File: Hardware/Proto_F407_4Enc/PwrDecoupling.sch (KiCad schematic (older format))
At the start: 35 parts, among them U2 AMS1117-3.3

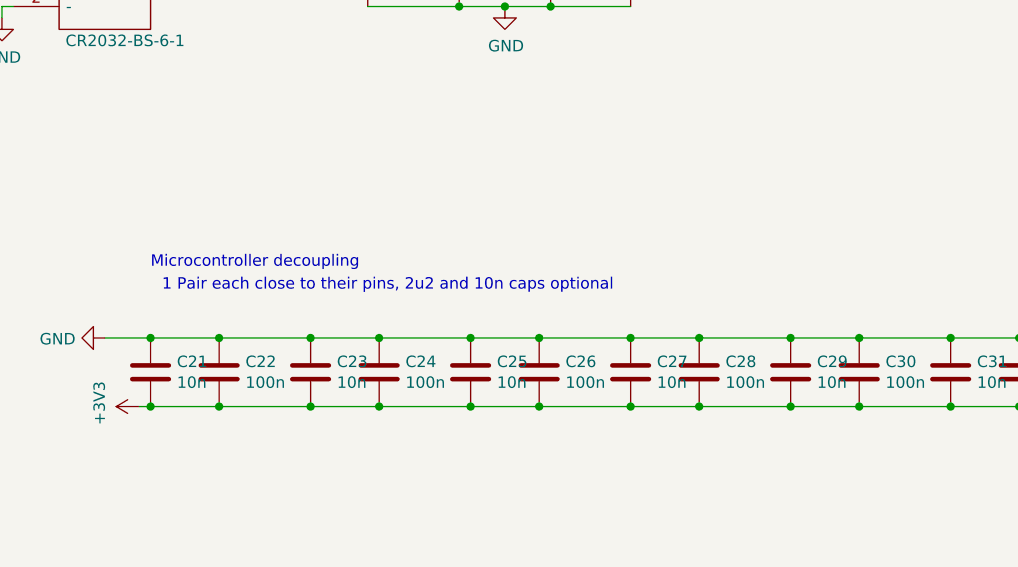
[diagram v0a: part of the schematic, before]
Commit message: minor label changes in schematic, added schematic + board image plots
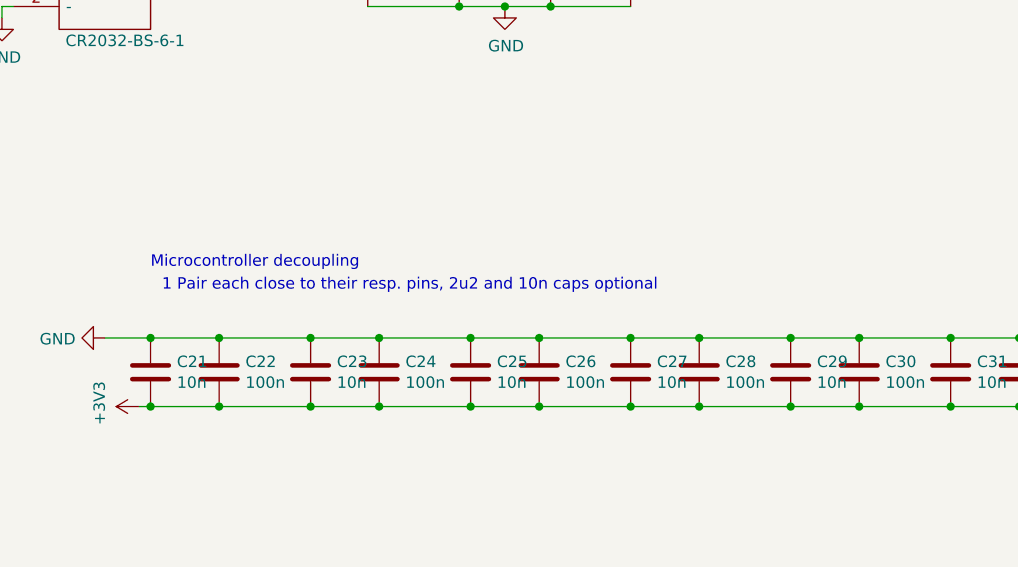
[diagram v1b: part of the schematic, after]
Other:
- note added: "1 Pair each close to their resp. pins, 2u2 and 10n caps optional"
- note removed: "1 Pair each close to their pins, 2u2 and 10n caps optional"
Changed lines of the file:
@@
 Microcontroller decoupling
 Text Notes 6400 4150 0    50   ~ 0
-1 Pair each close to their pins, 2u2 and 10n caps optional
+1 Pair each close to their resp. pins, 2u2 and 10n caps optional
 Text Notes 7200 1900 0    50   ~ 0
 VCAP
